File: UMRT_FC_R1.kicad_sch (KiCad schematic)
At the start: 1 part, among them J11 USB_A

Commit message: added some notes and PDF
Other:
- moved on the sheet: J11
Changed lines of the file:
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@@
 (kicad_sch (version 20230121) (generator eeschema)
   (paper "A4")
-  (no_connect (at 70.485 78.105))
+  (no_connect (at 95.885 78.105))
   (wire (pts (xy 158.75 106.045) (xy 171.45 106.045))
     (stroke (width 0) (type default))
@@
     (stroke (width 0) (type default))
   )
-  (wire (pts (xy 80.645 67.945) (xy 114.3 67.945))
-    (stroke (width 0) (type default))
-  )
   (wire (pts (xy 133.35 100.33) (xy 139.7 100.33))
     (stroke (width 0) (type default))
@@
     (stroke (width 0) (type default))
   )
-  (wire (pts (xy 81.915 61.595) (xy 81.915 62.865))
+  (wire (pts (xy 107.315 61.595) (xy 107.315 62.865))
     (stroke (width 0) (type default))
   )
-  (wire (pts (xy 73.025 78.105) (xy 73.025 79.375))
+  (wire (pts (xy 98.425 78.105) (xy 98.425 79.375))
     (stroke (width 0) (type default))
   )
@@
     (stroke (width 0) (type default))
   )
+  (wire (pts (xy 106.045 70.485) (xy 114.3 70.485))
+    (stroke (width 0) (type default))
+  )
   (wire (pts (xy 133.35 136.525) (xy 171.45 136.525))
     (stroke (width 0) (type default))
@@
     (stroke (width 0) (type default))
   )
-  (wire (pts (xy 80.645 70.485) (xy 114.3 70.485))
-    (stroke (width 0) (type default))
-  )
-  (wire (pts (xy 80.645 62.865) (xy 81.915 62.865))
+  (wire (pts (xy 106.045 62.865) (xy 107.315 62.865))
     (stroke (width 0) (type default))
   )
@@
     (stroke (width 0) (type default))
   )
+  (wire (pts (xy 106.045 67.945) (xy 114.3 67.945))
+    (stroke (width 0) (type default))
+  )
   (wire (pts (xy 158.75 78.74) (xy 171.45 78.74))
     (stroke (width 0) (type default))
   )
-  (symbol (lib_id "power:GND") (at 73.025 79.375 0) (unit 1)
+  (symbol (lib_id "power:GND") (at 98.425 79.375 0) (unit 1)
     (in_bom yes) (on_board yes) (dnp no) (fields_autoplaced)
-    (property "Reference" "#PWR058" (at 73.025 85.725 0)
+    (property "Reference" "#PWR058" (at 98.425 85.725 0)
       (effects (font (size 1.27 1.27)) hide)
     )
-    (property "Value" "GND" (at 73.025 83.82 0)
+    (property "Value" "GND" (at 98.425 83.82 0)
       (effects (font (size 1.27 1.27)))
     )
-    (property "Footprint" "" (at 73.025 79.375 0)
+    (property "Footprint" "" (at 98.425 79.375 0)
       (effects (font (size 1.27 1.27)) hide)
     )
-    (property "Datasheet" "" (at 73.025 79.375 0)
+    (property "Datasheet" "" (at 98.425 79.375 0)
       (effects (font (size 1.27 1.27)) hide)
     )
@@
     )
   )
-  (symbol (lib_id "power:VBUS") (at 81.915 61.595 0) (unit 1)
+  (symbol (lib_id "power:VBUS") (at 107.315 61.595 0) (unit 1)
     (in_bom yes) (on_board yes) (dnp no) (fields_autoplaced)
-    (property "Reference" "#PWR049" (at 81.915 65.405 0)
+    (property "Reference" "#PWR049" (at 107.315 65.405 0)
       (effects (font (size 1.27 1.27)) hide)
     )
-    (property "Value" "VBUS" (at 81.915 57.15 0)
+    (property "Value" "VBUS" (at 107.315 57.15 0)
       (effects (font (size 1.27 1.27)))
     )
-    (property "Footprint" "" (at 81.915 61.595 0)
+    (property "Footprint" "" (at 107.315 61.595 0)
       (effects (font (size 1.27 1.27)) hide)
     )
-    (property "Datasheet" "" (at 81.915 61.595 0)
+    (property "Datasheet" "" (at 107.315 61.595 0)
       (effects (font (size 1.27 1.27)) hide)
     )
@@
     )
   )
-  (symbol (lib_id "Connector:USB_A") (at 73.025 67.945 0) (unit 1)
+  (symbol (lib_id "Connector:USB_A") (at 98.425 67.945 0) (unit 1)
     (in_bom yes) (on_board yes) (dnp no) (fields_autoplaced)
-    (property "Reference" "J11" (at 73.025 55.88 0)
+    (property "Reference" "J11" (at 98.425 55.88 0)
       (effects (font (size 1.27 1.27)))
     )
-    (property "Value" "USB_A" (at 73.025 58.42 0)
+    (property "Value" "USB_A" (at 98.425 58.42 0)
       (effects (font (size 1.27 1.27)))
     )
-    (property "Footprint" "" (at 76.835 69.215 0)
+    (property "Footprint" "" (at 102.235 69.215 0)
       (effects (font (size 1.27 1.27)) hide)
     )
-    (property "Datasheet" " ~" (at 76.835 69.215 0)
+    (property "Datasheet" " ~" (at 102.235 69.215 0)
       (effects (font (size 1.27 1.27)) hide)
     )

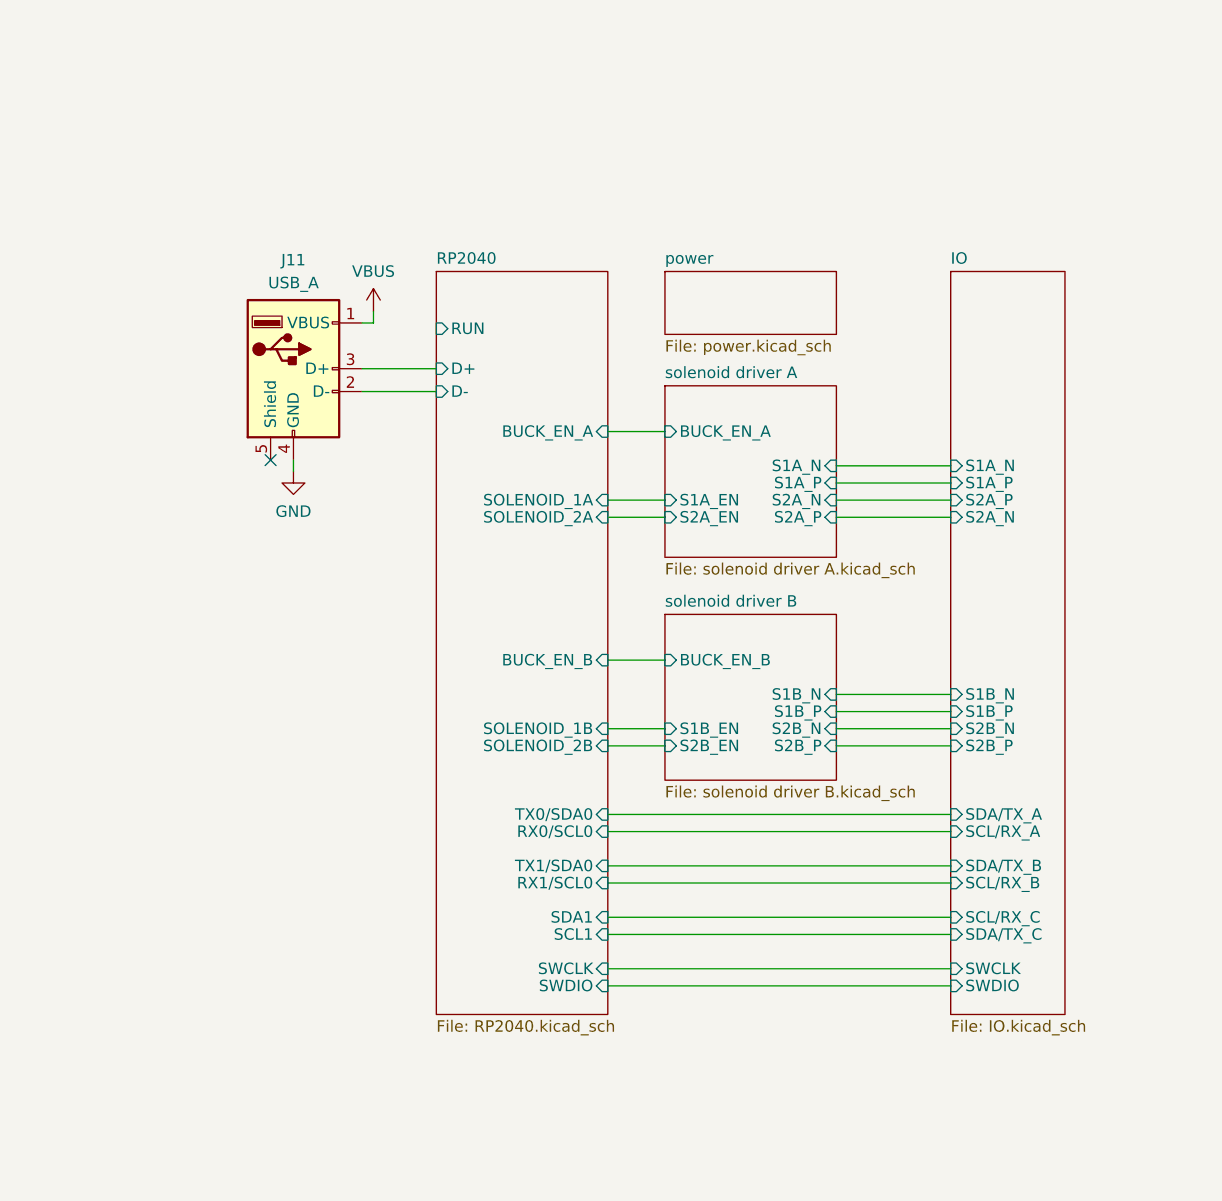
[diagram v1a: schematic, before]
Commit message: started on layout and added SD/flash/BNO
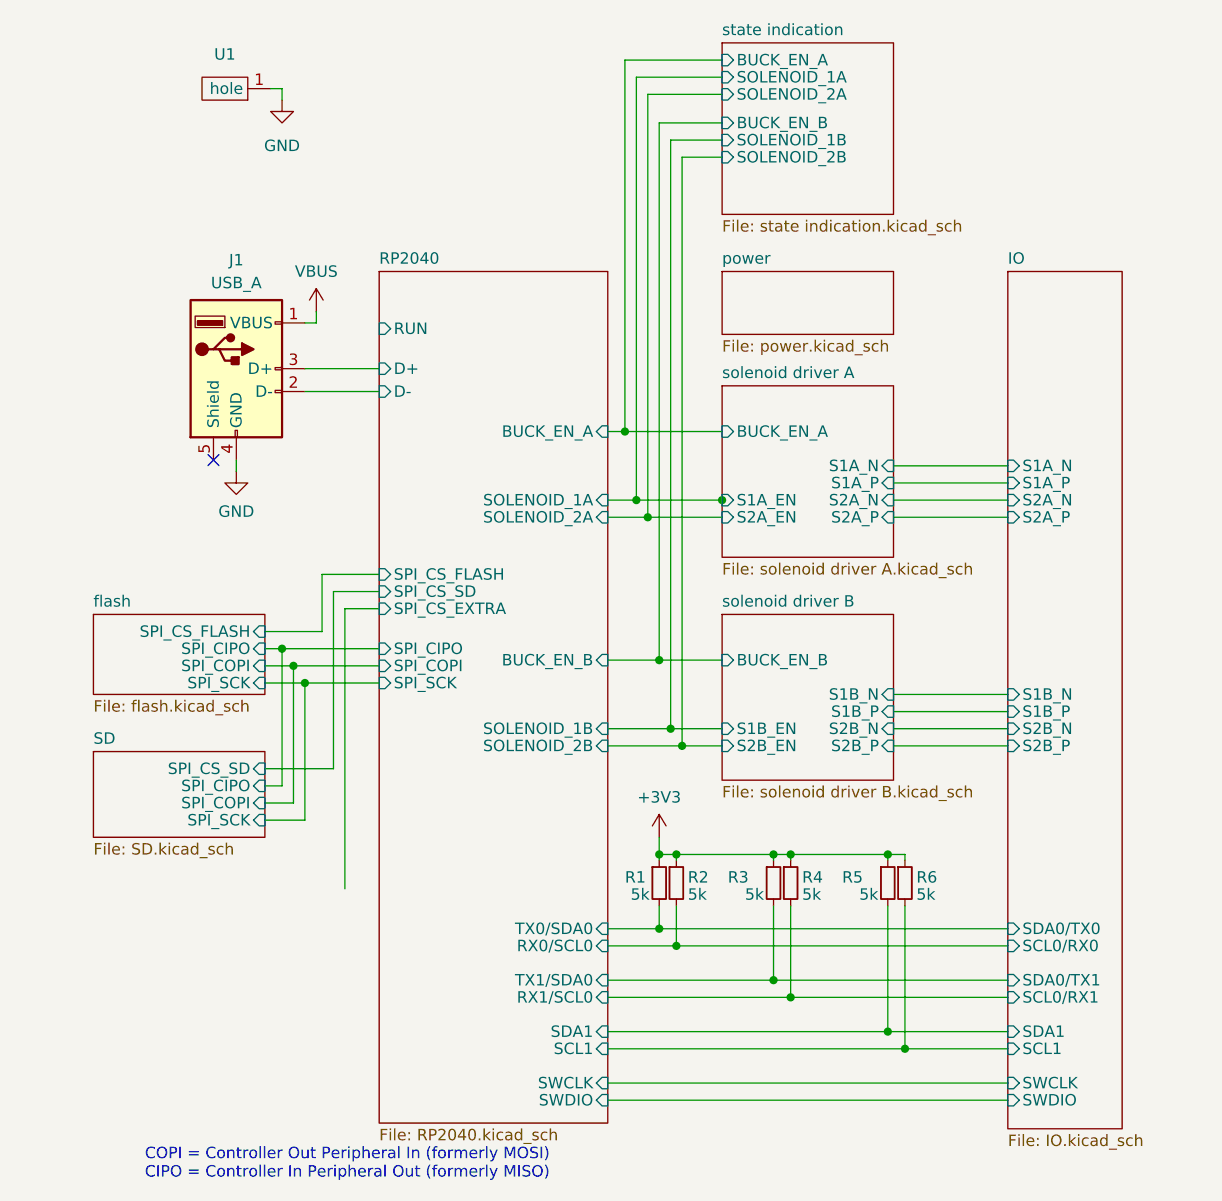
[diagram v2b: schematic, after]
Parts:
- added R1, R2, R3, R4, R5, R6: 5k, Resistor_SMD:R_0603_1608Metric, symbol Device:R_Small
- added U1: ~, ada_bno055:adafruit_bno055_nopins, symbol ada_bno055:ada_bno055_nopins
- J1: renamed from J11; footprint (none) -> Connector_USB:USB_Micro-B_Amphenol_10104110_Horizontal
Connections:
- net GND: now also U1.1 (hole)
- new net +3V3: R1.1, R2.1, R3.1, R4.1, R5.1, R6.1
- new net IO/SCL0/RX0: R2.2
- new net IO/SCL0/RX1: R4.2
- new net IO/SCL1: R6.2
- new net IO/SDA0/TX0: R1.2
- new net IO/SDA0/TX1: R3.2
- new net IO/SDA1: R5.2
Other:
- added sheet SD (SD.kicad_sch)
- added sheet flash (flash.kicad_sch)
- added sheet state indication (state indication.kicad_sch)
- sheet IO ports: added SCL0/RX0, SCL0/RX1, SCL1, SDA0/TX0, SDA0/TX1, SDA1; removed SCL/RX_A, SCL/RX_B, SCL/RX_C, SDA/TX_A, SDA/TX_B, SDA/TX_C
- sheet RP2040 ports: added SPI_CIPO, SPI_COPI, SPI_CS_EXTRA, SPI_CS_FLASH, SPI_CS_SD, SPI_SCK; removed none
- note added: "COPI = Controller Out Peripheral In (formerly MOSI) CIPO = Controller In Peripheral Out (formerly MISO)"
- moved on the sheet: J1
